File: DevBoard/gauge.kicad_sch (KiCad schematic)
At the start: 59 parts, among them J101 Pack (welded 4S) - use instea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, J102 Cell 1 NTC 10k 103AT, J103 EV2400 SMBus, J104 Bench PACK_P, J105 Cell 2 NTC 10k 103AT, J106 Cell 3 NTC 10k 103AT, J107 Cell 4 NTC 10k 103AT, Q101 AGM404AP1, Q102 AGM404AP1, Q103 BSS138, SW101 WAKE, U101 BQ40Z50RSMR-R2

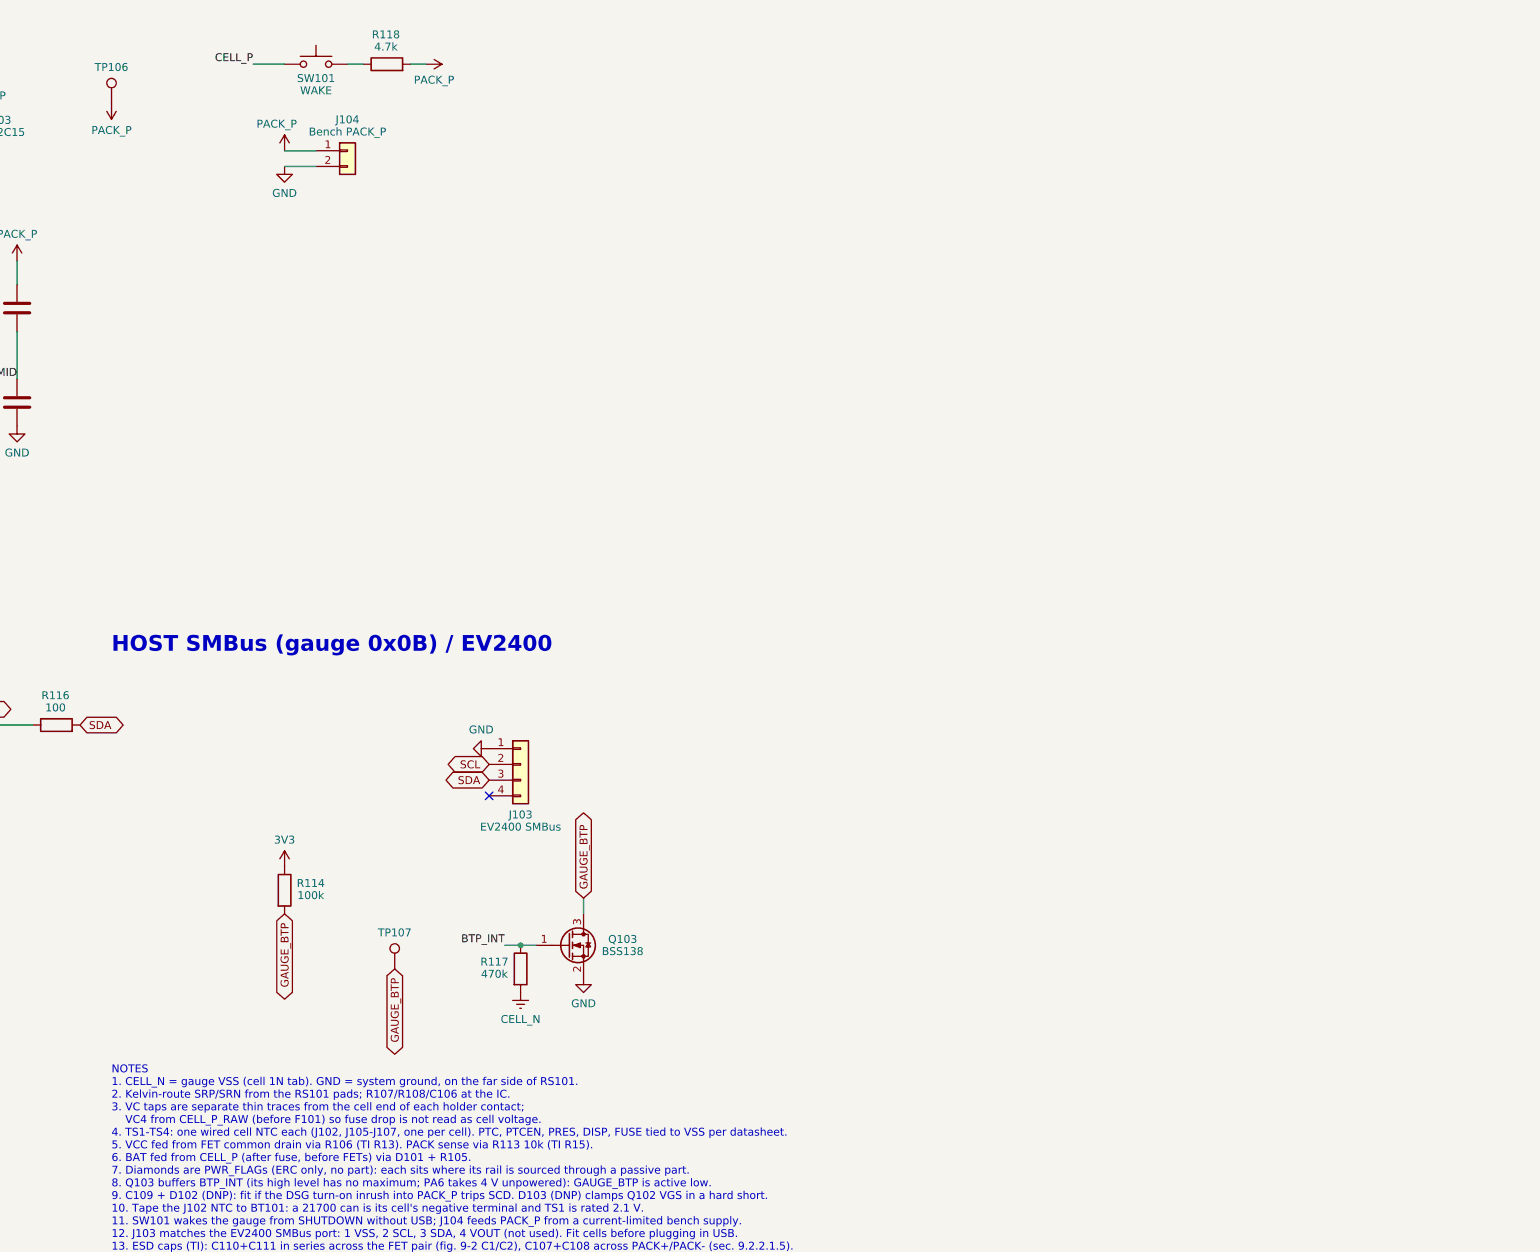
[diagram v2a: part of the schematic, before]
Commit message: Dev board: open-item pass, J104 diode, antenna keep-out, bring-up checklist
- D104 SS34 in series with the J104 bench input (reversed lead, back-feed).
- ANT_KEEPOUT rule area (no tracks/vias/pours, all copper layers) around
  the STM32WB1MMC antenna end, created by place_parts.py.
- D401 drawn unidirectional; header part numbers (PZ254V-11 family);
  shunt, J301 keying, B-constant, insulated-NTC, sheet-text and R201 notes.
- docs/devboard/bringup-config-checklist.md: every configuration item from
  both reviews in bring-up order, with review 2's precharge correction;
  review 1's 0 mV precharge line marked superseded.

Co-Authored-By: Claude Opus 5.5 <noreply@anthropic.com>
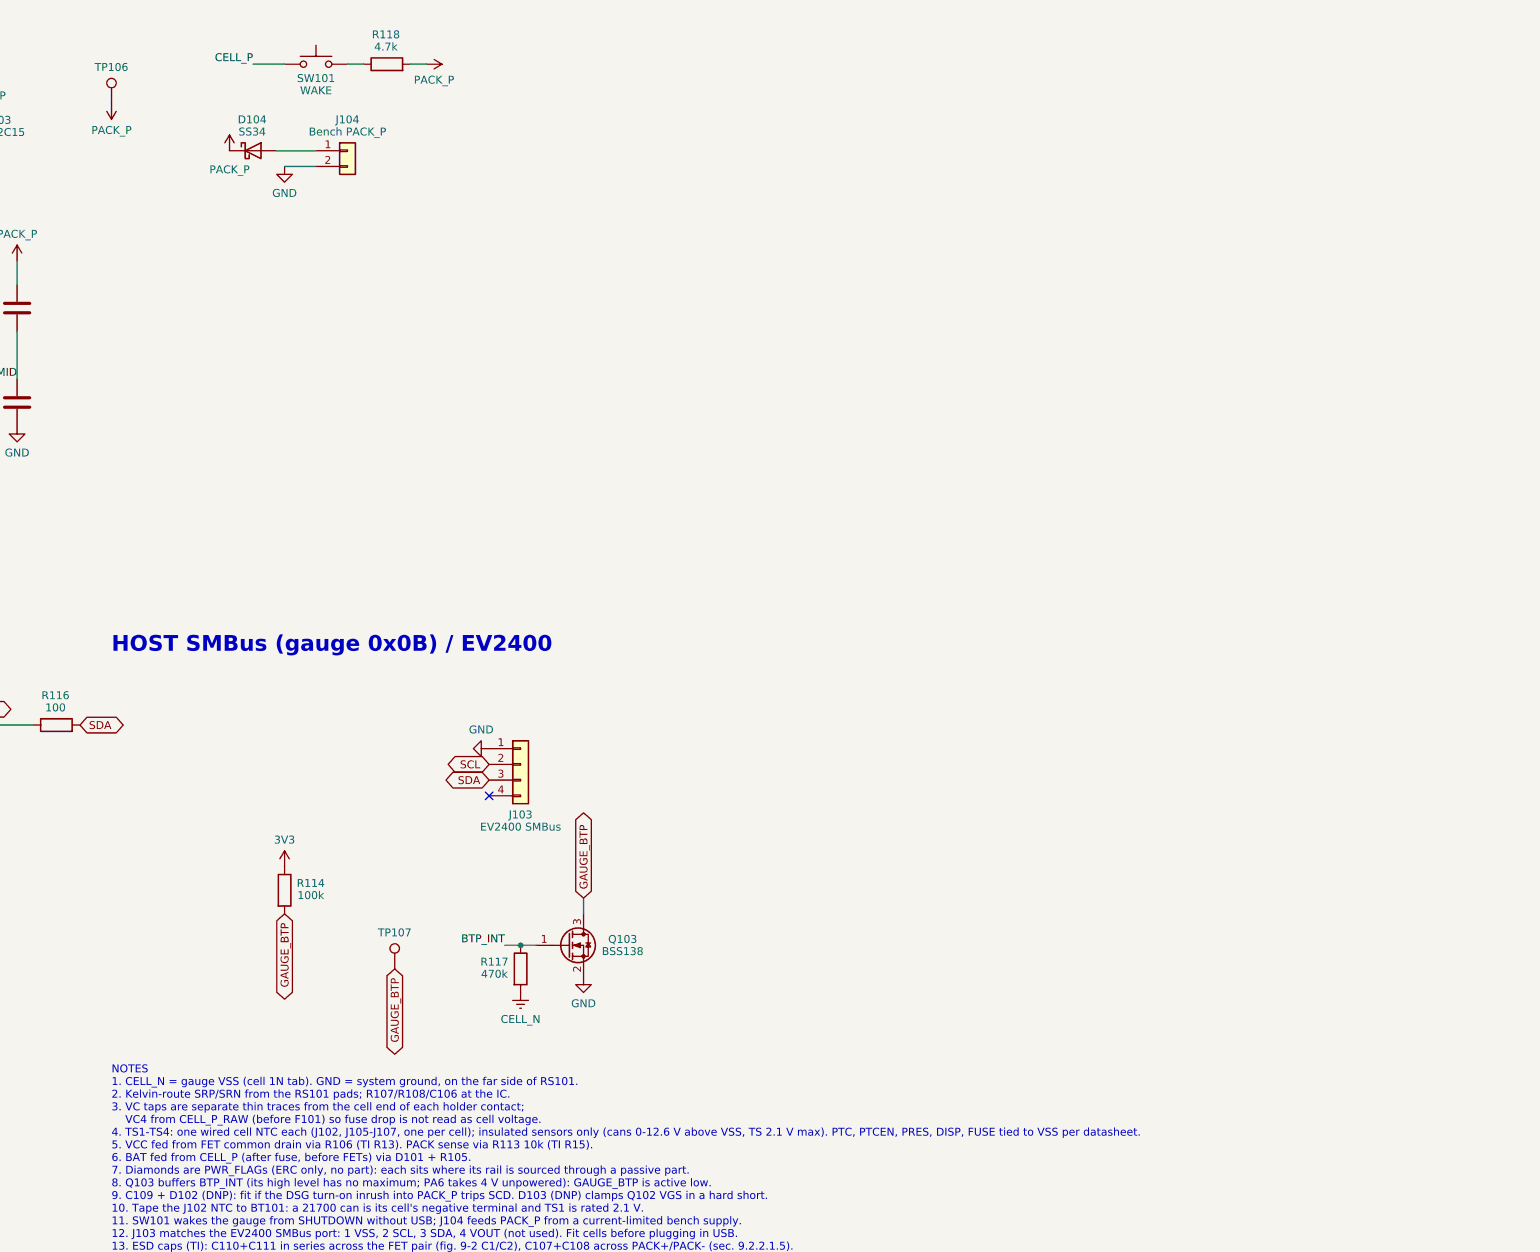
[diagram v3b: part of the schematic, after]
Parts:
- added D104: SS34, Diode_SMD:D_SMA, symbol Device:D_Schottky
- J103: LCSC (none) -> C2691448; MPN (none) -> PZ254V-11-04P
- J104: Notes Bench supply onto PACK_P (gauge wake, EV2400 work with FETs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 -> Bench supply onto PACK_P through D104 (gauge wake, EV2400 w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
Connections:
- net PACK_P: now also D104.1 (K); no longer J104.1 (Pin_1)
- new net: D104.2 (A), J104.1 (Pin_1)
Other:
- note added: "NOTES 1. CELL_N = gauge VSS (cell 1N tab). GND = system ground, on the far side of RS101. 2. Kelvin-route SRP/SRN from the RS101 pads; R107/R108/C106 at the IC. 3. VC taps are separate thin traces from the cell end of each holder contact; VC4 from CELL_P_RAW (before F101) so fuse drop is not read as cell voltage. 4. TS1-TS4: one wired cell NTC each (J102, J105-J107, one per cell); insulated senso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"
- note removed: "NOTES 1. CELL_N = gauge VSS (cell 1N tab). GND = system ground, on the far side of RS101. 2. Kelvin-route SRP/SRN from the RS101 pads; R107/R108/C106 at the IC. 3. VC taps are separate thin traces from the cell end of each holder contact; VC4 from CELL_P_RAW (before F101) so fuse drop is not read as cell voltage. 4. TS1-TS4: one wired cell NTC each (J102, J105-J107, one per cell). PTC, PTCEN, PRE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"
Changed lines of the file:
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@@
 		)
 	)
-	(text "NOTES\n1. CELL_N = gauge VSS (cell 1N tab). GND = system ground, on the far side of RS101.\n2. Kelvin-route SRP/SRN from the RS101 pads; R107/R108/C106 at the IC.\n3. VC taps are separate thin traces from the cell end of each holder contact;\n    VC4 from CELL_P_RAW (before F101) so fuse drop is not read as cell voltage.\n4. TS1-TS4: one wired cell NTC each (J102, J105-J107, one per cell). PTC, PTCEN, PRES, DISP, FUSE tied to VSS per datasheet.\n5. VCC fed from FET common drain via R106 (TI R13). PACK sense via R113 10k (TI R15).\n6. BAT fed from CELL_P (after fuse, before FETs) via D101 + R105.\n7. Diamonds are PWR_FLAGs (ERC only, no part): each sits where its rail is sourced through a passive part.\n8. Q103 buffers BTP_INT (its high level has no maximum; PA6 takes 4 V unpowered): GAUGE_BTP is active low.\n9. C109 + D102 (DNP): fit if the DSG turn-on inrush into PACK_P trips SCD. D103 (DNP) clamps Q102 VGS in a hard short.\n10. Tape the J102 NTC to BT101: a 21700 can is its cell's negative terminal and TS1 is rated 2.1 V.\n11. SW101 wakes the gauge from SHUTDOWN without USB; J104 feeds PACK_P from a current-limited bench supply.\n12. J103 matches the EV2400 SMBus port: 1 VSS, 2 SCL, 3 SDA, 4 VOUT (not used). Fit cells before plugging in USB.\n13. ESD caps (TI): C110+C111 in series across the FET pair (fig. 9-2 C1/C2), C107+C108 across PACK+/PACK- (sec. 9.2.2.1.5)."
+	(text "NOTES\n1. CELL_N = gauge VSS (cell 1N tab). GND = system ground, on the far side of RS101.\n2. Kelvin-route SRP/SRN from the RS101 pads; R107/R108/C106 at the IC.\n3. VC taps are separate thin traces from the cell end of each holder contact;\n    VC4 from CELL_P_RAW (before F101) so fuse drop is not read as cell voltage.\n4. TS1-TS4: one wired cell NTC each (J102, J105-J107, one per cell); insulated sensors only (cans 0-12.6 V above VSS, TS 2.1 V max). PTC, PTCEN, PRES, DISP, FUSE tied to VSS per datasheet.\n5. VCC fed from FET common drain via R106 (TI R13). PACK sense via R113 10k (TI R15).\n6. BAT fed from CELL_P (after fuse, before FETs) via D101 + R105.\n7. Diamonds are PWR_FLAGs (ERC only, no part): each sits where its rail is sourced through a passive part.\n8. Q103 buffers BTP_INT (its high level has no maximum; PA6 takes 4 V unpowered): GAUGE_BTP is active low.\n9. C109 + D102 (DNP): fit if the DSG turn-on inrush into PACK_P trips SCD. D103 (DNP) clamps Q102 VGS in a hard short.\n10. Tape the J102 NTC to BT101: a 21700 can is its cell's negative terminal and TS1 is rated 2.1 V.\n11. SW101 wakes the gauge from SHUTDOWN without USB; J104 feeds PACK_P from a current-limited bench supply.\n12. J103 matches the EV2400 SMBus port: 1 VSS, 2 SCL, 3 SDA, 4 VOUT (not used). Fit cells before plugging in USB.\n13. ESD caps (TI): C110+C111 in series across the FET pair (fig. 9-2 C1/C2), C107+C108 across PACK+/PACK- (sec. 9.2.2.1.5)."
 		(exclude_from_sim no)
 		(at 266.7 236.22 0)
@@
 	(wire
 		(pts
-			(xy 186.69 33.02) (xy 189.23 33.02)
+			(xy 293.37 58.42) (xy 299.72 58.42)
 		)
 		(stroke
@@
 	(wire
 		(pts
-			(xy 176.53 33.02) (xy 179.07 33.02)
+			(xy 186.69 33.02) (xy 189.23 33.02)
 		)
 		(stroke
@@
 	(wire
 		(pts
-			(xy 168.91 33.02) (xy 166.37 33.02)
+			(xy 176.53 33.02) (xy 179.07 33.02)
 		)
 		(stroke
@@
 	(wire
 		(pts
-			(xy 299.72 60.96) (xy 294.64 60.96)
+			(xy 168.91 33.02) (xy 166.37 33.02)
 		)
 		(stroke
@@
 	(wire
 		(pts
-			(xy 299.72 58.42) (xy 294.64 58.42)
+			(xy 299.72 60.96) (xy 294.64 60.96)
 		)
 		(stroke
@@
 			)
 		)
+		(property "LCSC" "C2691448"
+			(at 332.74 157.48 0)
+			(hide yes)
+			(show_name no)
+			(do_not_autoplace no)
+			(effects
+				(font
+					(size 1.27 1.27)
+				)
+			)
+		)
+		(property "MPN" "PZ254V-11-04P"
+			(at 332.74 157.48 0)
+			(hide yes)
+			(show_name no)
+			(do_not_autoplace no)
+			(effects
+				(font
+					(size 1.27 1.27)
+				)
+			)
+		)
 		(pin "1"
 		)
@@
 			)
 		)
-		(property "Notes" "Bench supply onto PACK_P (gauge wake, EV2400 work with FETs off). Current-limit the supply"
+		(property "Notes" "Bench supply onto PACK_P through D104 (gauge wake, EV2400 work with FETs off). Current-limit the supply; D104 blocks a reversed lead and keeps PACK_P off the header"
 			(at 304.8 58.42 0)
 			(hide yes)
@@
 	(symbol
 		(lib_id "power:VCC")
-		(at 294.64 58.42 0)
+		(at 285.75 58.42 0)
 		(unit 1)
 		(body_style 1)
@@
 		)
 		(property "Value" "PACK_P"
-			(at 293.37 54.10 0)
+			(at 285.75 61.47 0)
 			(show_name no)
 			(do_not_autoplace no)
@@
 		)
 		(property "Footprint" ""
-			(at 294.64 58.42 0)
+			(at 285.75 58.42 0)
 			(hide yes)
 			(show_name no)
@@
 		)
 		(property "Datasheet" ""
-			(at 294.64 58.42 0)
+			(at 285.75 58.42 0)
 			(hide yes)
 			(show_name no)
@@
 		)
 		(property "Description" ""
-			(at 294.64 58.42 0)
+			(at 285.75 58.42 0)
 			(hide yes)
 			(show_name no)
@@
 					(unit 1)
 				)
+			)
+		)
+	)
+	(symbol
+		(lib_id "Device:D_Schottky")
+		(at 289.56 58.42 0)
+		(unit 1)
+		(body_style 1)
+		(exclude_from_sim no)
+		(in_bom yes)
+		(on_board yes)
+		(in_pos_files yes)
+		(dnp no)
+		(property "Reference" "D104"
+			(at 289.41 53.40 0)
+			(show_name no)
+			(do_not_autoplace no)
+			(effects
+				(font
+					(size 1.27 1.27)
+				)
+			)
+		)
+		(property "Value" "SS34"
+			(at 289.41 55.37 0)
+			(show_name no)
+			(do_not_autoplace no)
+			(effects
+				(font
+					(size 1.27 1.27)
+				)
+			)
+		)
+		(property "Footprint" "Diode_SMD:D_SMA"
+			(at 289.56 58.42 0)
+			(hide yes)
+			(show_name no)
+			(do_not_autoplace no)
+			(effects
+				(font
+					(size 1.27 1.27)
+				)
+			)
+		)
+		(property "Datasheet" ""
+			(at 289.56 58.42 0)
+			(hide yes)
+			(show_name no)
+			(do_not_autoplace no)
+			(effects
+				(font
+					(size 1.27 1.27)
+				)
+			)
+		)
+		(property "Description" ""
+			(at 289.56 58.42 0)
+			(hide yes)
+			(show_name no)
+			(do_not_autoplace no)
+			(effects
+				(font
+					(size 1.27 1.27)
+				)
+			)
+		)
+		(property "LCSC" "C8678"
+			(at 289.56 58.42 0)
+			(hide yes)
+			(show_name no)
+			(do_not_autoplace no)
+			(effects
+				(font
+					(size 1.27 1.27)
+				)
+			)
+		)
+		(property "MPN" "SS34 (MDD)"
+			(at 289.56 58.42 0)
+			(hide yes)
+			(show_name no)
+			(do_not_autoplace no)
+			(effects
+				(font
+					(size 1.27 1.27)
+				)
+			)
+		)
+		(property "Notes" "J104 series diode: a reversed bench lead cannot drive PACK_P negative (TI 9.2.2.3.3), and a live PACK_P (up to 16.8 V) does not appear on the bare header pins. ~0.4 V drop at bench currents"
+			(at 289.56 58.42 0)
+			(hide yes)
+			(show_name no)
+			(do_not_autoplace no)
+			(effects
+				(font
+					(size 1.27 1.27)
+				)
+			)
+		)
+		(pin "1"
+		)
+		(pin "2"
+		)
+		(instances
+			(project "MonolithDev"
+				(path "/f83241ae-2bb3-4ed7-b986-c0a03971de0a/5f8e2264-136e-4c01-877f-88ca3aa05650"
+					(reference "D104")
+					(unit 1)
+				)

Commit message: Dev board: second-level pack protection, D103 fitted, U202 JLC, strap cleanup
- Gauge sheet: BQ294700 (4.35 V/cell OVP) and the BQ40Z50 FUSE pin share
  ignition FET Q104 (TI BQ40Z50-R2 fig. 9-11) to blow F102, a TLC WSFB1514
  4-cell 15 A self-control fuse at the cell top. F101 removed: F102 is the
  pack fuse. R127 DNP bench bypass. New symbols/footprint/3D model.
- D103 (Q102 gate-source 15 V clamp) fitted on dev board and production.
- U202 INA190A1 now JLC-assembled (C1852068); U201 stays hand-soldered.
- TPS25751 ADCIN divider footprints R405-R408 removed (SafeMode 0x20/0x21
  needs only the R1-R4 ties); place_parts rows and notes updated.
- Layout not yet updated for these changes.

Co-Authored-By: Claude Opus 5.5 <noreply@anthropic.com>
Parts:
- removed F101: 15A 32V, Fuse:Fuse_1206_3216Metric, symbol Device:Fuse
- added C112, C113, C114, C115, C116, C117, C118: 0.1u 50V, Capacitor_SMD:C_0603_1608Metric, symbol Device:C
- added F102: WSFB1514, MonolithDev:TLC_WSFB_4x3mm, symbol MonolithDev:WSFB1514
- added Q104: AO3400A, Package_TO_SOT_SMD:SOT-23, symbol Transistor_FET:Q_NMOS_GSD
- added R119, R120, R121, R122: 1k, Resistor_SMD:R_0603_1608Metric, symbol Device:R
- added R123: 100, Resistor_SMD:R_0603_1608Metric, symbol Device:R
- added R124, R126: 5.1k, Resistor_SMD:R_0603_1608Metric, symbol Device:R
- added R125: 51k, Resistor_SMD:R_0603_1608Metric, symbol Device:R
- added R127: 0R DNP, Resistor_SMD:R_2512_6332Metric, symbol Device:R
- added U102: BQ294700DSGR, Package_SON:Texas_DSG0008A_WSON-8-1EP_2x2mm_P0.5mm_EP0.9x1.6mm, symbol MonolithDev:BQ294700
- C109: Notes DNP: fit only if DSG turn-on inrush trips SCD. 4.7 nF (not 0.1 uF) keeps the short-circuit turn-off fast enough for Q102 SOA (review 2 A-2). Fit D103 (VGS clamp) whenever C109 is fitted -> DNP: fit only if DSG turn-on inrush trips SCD. 4.7 nF (not 0.1 uF) keeps the short-circuit turn-off fast enough for Q102 SOA (review 2 A-2). D103 (VGS clamp, now always fitted) covers it
- D101: Notes BAT feed from the cell top before F101, as TI fig. 9-12 (D1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 -> BAT feed from the cell top before F102, as TI fig. 9-12 (D1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
- D103: Notes DNP: clamps Q102 VGS (+/-20 V) if a hard PACK_P short outla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 -> Fitted (2026-10-13, dev board and production): clamps Q102 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; now fitted
- TP108: Notes Cell top before F101: check BT104 / the stack before fittin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 -> Cell top, before F102: check BT104 / the stack here
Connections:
- net CELL1: now also R122.1
- net CELL2: now also R121.1
- net CELL3: now also R120.1
- net CELL_N: now also C115.2, C116.2, C117.1, C118.2, Q104.2 (S), R125.2, U102.6 (VSS), U102.9 (VSS); no longer U101.25 (FUSE)
- net CELL_P: now also F102.2, R127.2
- net CELL_P_RAW: now also F102.1, R119.1, R123.2, R127.1
- new net: C118.1, Q104.1 (G), R124.2, R125.1, R126.1
- new net: C112.2, C113.1, R120.2, U102.3 (V3)
- new net: C113.2, C114.1, R121.2, U102.4 (V2)
- new net: C116.1, R123.1, U102.1 (VDD)
- new net: R124.1, U102.8 (OUT)
- new net: C114.2, C115.1, R122.2, U102.5 (V1)
- new net: C112.1, R119.2, U102.2 (V4)
- new net: C117.2, U102.7 (CD)
- new net: F102.3 (HTR), Q104.3 (D)
- new net GAUGE_FUSE: R126.2, U101.25 (FUSE)
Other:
- note added: "NOTES 1. CELL_N = gauge VSS (cell 1N tab). GND = system ground, on the far side of RS101. 2. Kelvin-route SRP/SRN from the RS101 pads; R107/R108/C106 at the IC. 3. VC taps are separate thin traces from the cell end of each holder contact; VC4 from CELL_P_RAW (before F102) so fuse drop is not read as cell voltage. 4. TS1-TS4: one wired cell NTC each (J102, J105-J107, one per cell); insulated senso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"
- note added: "SECOND-LEVEL PROTECTION BQ294700 + SCP (TI fig. 9-11)"
- note removed: "NOTES 1. CELL_N = gauge VSS (cell 1N tab). GND = system ground, on the far side of RS101. 2. Kelvin-route SRP/SRN from the RS101 pads; R107/R108/C106 at the IC. 3. VC taps are separate thin traces from the cell end of each holder contact; VC4 from CELL_P_RAW (before F101) so fuse drop is not read as cell voltage. 4. TS1-TS4: one wired cell NTC each (J102, J105-J107, one per cell); insulated senso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"
